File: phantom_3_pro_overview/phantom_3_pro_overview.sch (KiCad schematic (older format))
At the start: 11 parts, among them M1 Brushless_Motor_3phase_seri, M2 Brushless_Motor_3phase_seri, M3 Brushless_Motor_3phase_seri, M4 Brushless_Motor_3phase_seri

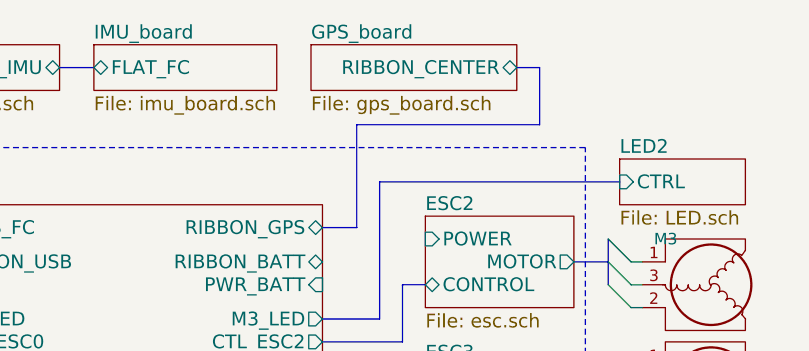
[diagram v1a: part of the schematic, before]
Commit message: Overview: Conceptual schematics of some components.
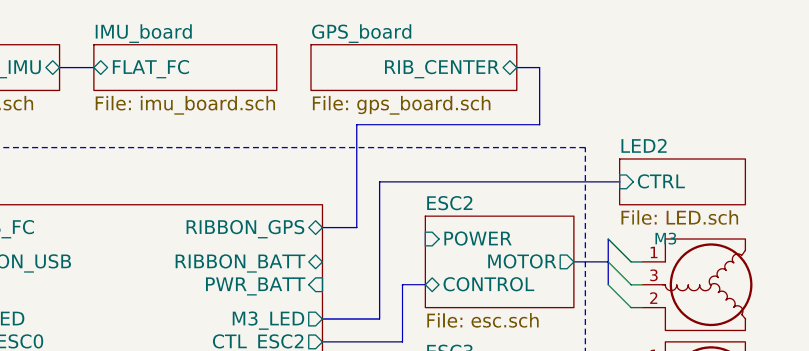
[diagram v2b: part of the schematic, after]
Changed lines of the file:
@@
 LIBS:valves
 LIBS:motors
+LIBS:ic_dil_generic
+LIBS:sensors
+LIBS:u-blox
+LIBS:amplifiers
 LIBS:phantom_3_pro_overview-cache
 EELAYER 25 0
@@
 F0 "GPS_board" 60
 F1 "gps_board.sch" 60
-F2 "RIBBON_CENTER" B R 5000 750 60
+F2 "RIB_CENTER" B R 5000 750 60
 $EndSheet
 $Sheet
@@
 F1 "imu_board.sch" 60
 F2 "FLAT_FC" B L 3150 750 60
-$EndSheet
-$Sheet
-S 1350 1400 650  400
-U 596D582B
-F0 "ESC0" 60
-F1 "esc.sch" 60
-F2 "CONTROL" B R 2000 1700 60
-F3 "POWER" I R 2000 1500 60
-F4 "MOTOR" O L 1350 1600 60
 $EndSheet
 $Sheet
@@
 F3 "FLAT_MOTOR" O L 1700 4600 60
 $EndSheet
+$Sheet
+S 1350 1400 650  400
+U 596D582B
+F0 "ESC0" 60
+F1 "esc.sch" 60
+F2 "CONTROL" B R 2000 1700 60
+F3 "POWER" I R 2000 1500 60
+F4 "MOTOR" O L 1350 1600 60
+$EndSheet
 $EndSCHEMATC

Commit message: Overview: Work on camera and gimbal.
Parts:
- removed M_pitch, M_roll, M_yaw: Motor_Servo, symbol Motor_Servo
- added M_pitch, M_roll, M_yaw: Motor_Servo_3Ph, symbol Motor_Servo_3Ph
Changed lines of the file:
@@
 LIBS:amplifiers
 LIBS:transistors-switches
+LIBS:transistors-power
 LIBS:phantom_3_pro_overview-cache
 EELAYER 25 0
@@
 Entry Bus Bus
 	1400 3000 1500 2900
-$Comp
-L Motor_Servo M_pitch
-U 1 1 5970AE18
-P 1000 5350
-F 0 "M_pitch" H 800 5525 50  0000 L CNN
-F 1 "Motor_Servo" H 800 5190 50  0000 L TNN
-F 2 "" H 1000 5160 50  0001 C CNN
-F 3 "" H 1000 5160 50  0001 C CNN
-	1    1000 5350
-	-1   0    0    1
-$EndComp
 Entry Wire Line
 	1450 5550 1350 5450
@@
 Wire Bus Line
 	1450 5600 1550 5600
-$Comp
-L Motor_Servo M_roll
-U 1 1 5970C2E7
-P 1000 4900
-F 0 "M_roll" H 800 5075 50  0000 L CNN
-F 1 "Motor_Servo" H 800 4740 50  0000 L TNN
-F 2 "" H 1000 4710 50  0001 C CNN
-F 3 "" H 1000 4710 50  0001 C CNN
-	1    1000 4900
-	-1   0    0    1
-$EndComp
 Entry Wire Line
 	1450 5100 1350 5000
@@
 Wire Bus Line
 	1450 5150 1550 5150
-$Comp
-L Motor_Servo M_yaw
-U 1 1 5970C4FE
-P 1000 4350
-F 0 "M_yaw" H 800 4525 50  0000 L CNN
-F 1 "Motor_Servo" H 800 4190 50  0000 L TNN
-F 2 "" H 1000 4160 50  0001 C CNN
-F 3 "" H 1000 4160 50  0001 C CNN
-	1    1000 4350
-	-1   0    0    1
-$EndComp
 Entry Wire Line
 	1450 4550 1350 4450
@@
 Wire Bus Line
 	3300 4450 3150 4450
+$Comp
+L Motor_Servo_3Ph M_yaw
+U 1 1 59719EE0
+P 1000 4350
+F 0 "M_yaw" H 800 4525 50  0000 L CNN
+F 1 "Motor_Servo_3Ph" H 800 4190 50  0000 L TNN
+F 2 "" H 1000 4160 50  0001 C CNN
+F 3 "" H 1000 4160 50  0001 C CNN
+	1    1000 4350
+	-1   0    0    1
+$EndComp
+$Comp
+L Motor_Servo_3Ph M_roll
+U 1 1 5971A5AD
+P 1000 4900
+F 0 "M_roll" H 800 5075 50  0000 L CNN
+F 1 "Motor_Servo_3Ph" H 800 4740 50  0000 L TNN
+F 2 "" H 1000 4710 50  0001 C CNN
+F 3 "" H 1000 4710 50  0001 C CNN
+	1    1000 4900
+	-1   0    0    1
+$EndComp
+$Comp
+L Motor_Servo_3Ph M_pitch
+U 1 1 5971A85D
+P 1000 5350
+F 0 "M_pitch" H 800 5525 50  0000 L CNN
+F 1 "Motor_Servo_3Ph" H 800 5190 50  0000 L TNN
+F 2 "" H 1000 5160 50  0001 C CNN
+F 3 "" H 1000 5160 50  0001 C CNN
+	1    1000 5350
+	-1   0    0    1
+$EndComp
 $EndSCHEMATC

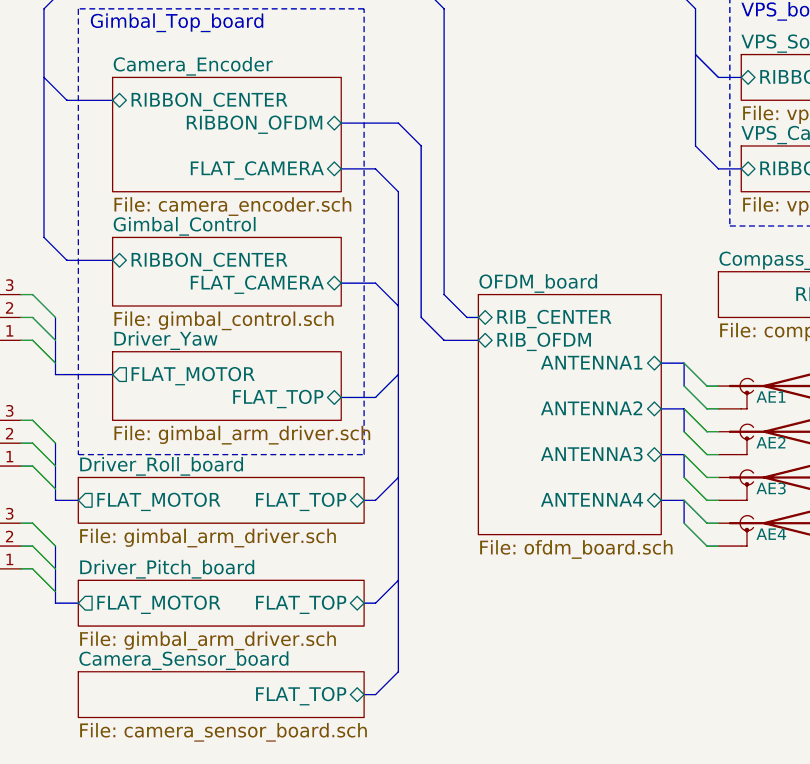
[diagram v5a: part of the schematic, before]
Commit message: Overview: Updated to latest findings.
Added magnetometer to gimbal control, and made some minor fixes.
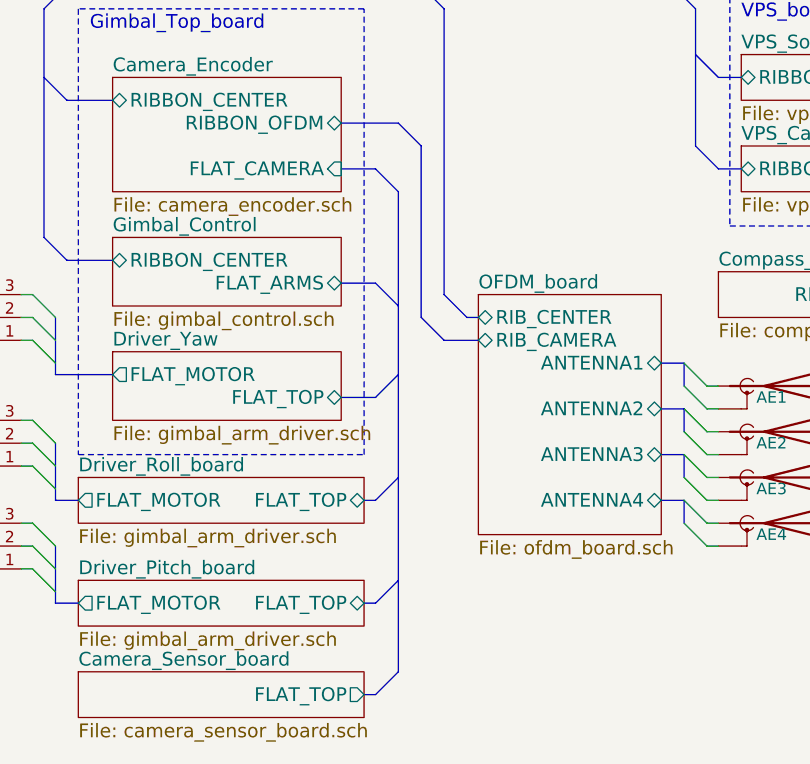
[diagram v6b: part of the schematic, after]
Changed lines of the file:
@@
 F1 "ofdm_board.sch" 60
 F2 "RIB_CENTER" B L 3300 4350 60
-F3 "RIB_OFDM" B L 3300 4450 60
-F4 "ANTENNA1" B R 4100 4550 60
-F5 "ANTENNA2" B R 4100 4750 60
-F6 "ANTENNA3" B R 4100 4950 60
-F7 "ANTENNA4" B R 4100 5150 60
+F3 "ANTENNA1" B R 4100 4550 60
+F4 "ANTENNA2" B R 4100 4750 60
+F5 "ANTENNA3" B R 4100 4950 60
+F6 "ANTENNA4" B R 4100 5150 60
+F7 "RIB_CAMERA" B L 3300 4450 60
 $EndSheet
 $Sheet
@@
 F2 "RIBBON_CENTER" B L 1700 3400 60
 F3 "RIBBON_OFDM" B R 2700 3500 60
-F4 "FLAT_CAMERA" B R 2700 3700 60
+F4 "FLAT_CAMERA" I R 2700 3700 60
 $EndSheet
 $Sheet
@@
 F1 "gimbal_control.sch" 60
 F2 "RIBBON_CENTER" B L 1700 4100 60
-F3 "FLAT_CAMERA" B R 2700 4200 60
+F3 "FLAT_ARMS" B R 2700 4200 60
 $EndSheet
 $Sheet
@@
 F0 "Camera_Sensor_board" 60
 F1 "camera_sensor_board.sch" 60
-F2 "FLAT_TOP" B R 2800 6000 60
+F2 "FLAT_TOP" O R 2800 6000 60
 $EndSheet
 $Comp

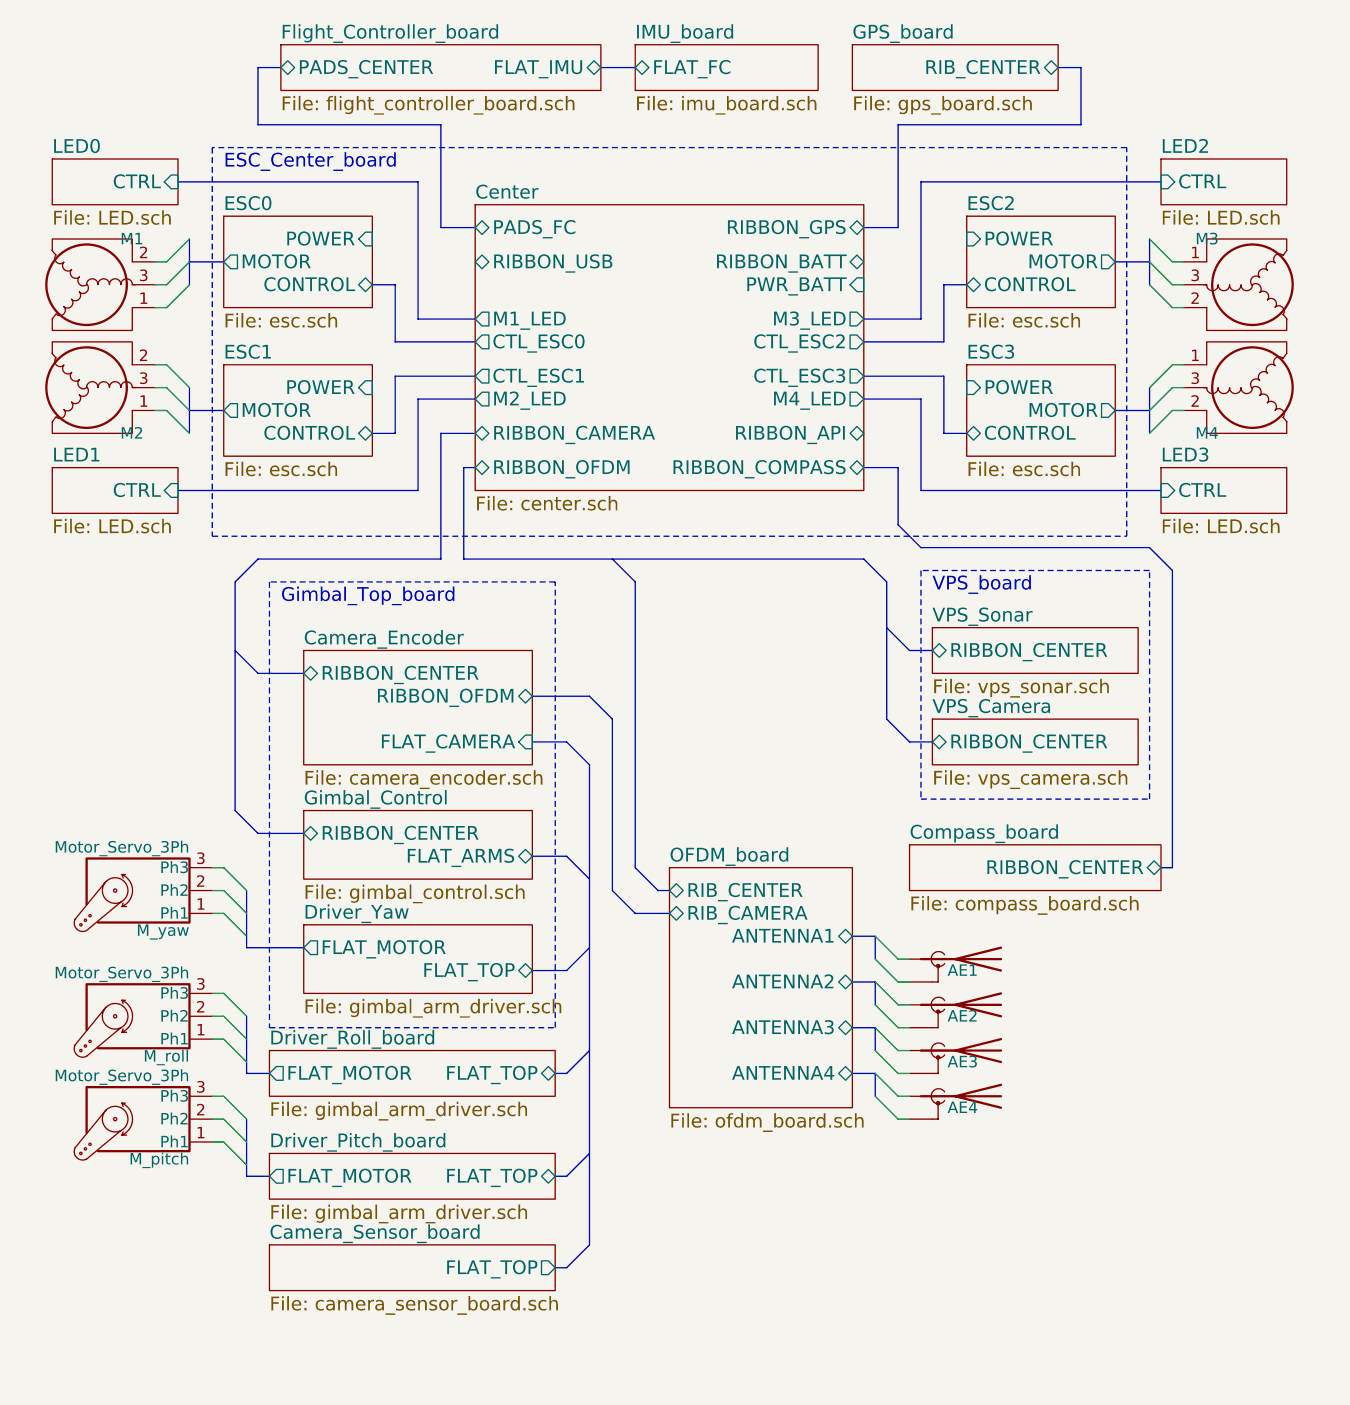
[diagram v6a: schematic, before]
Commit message: Overview: Separated gimbal power circuit.
This is to make sure the connection won't be interpreted as data link.
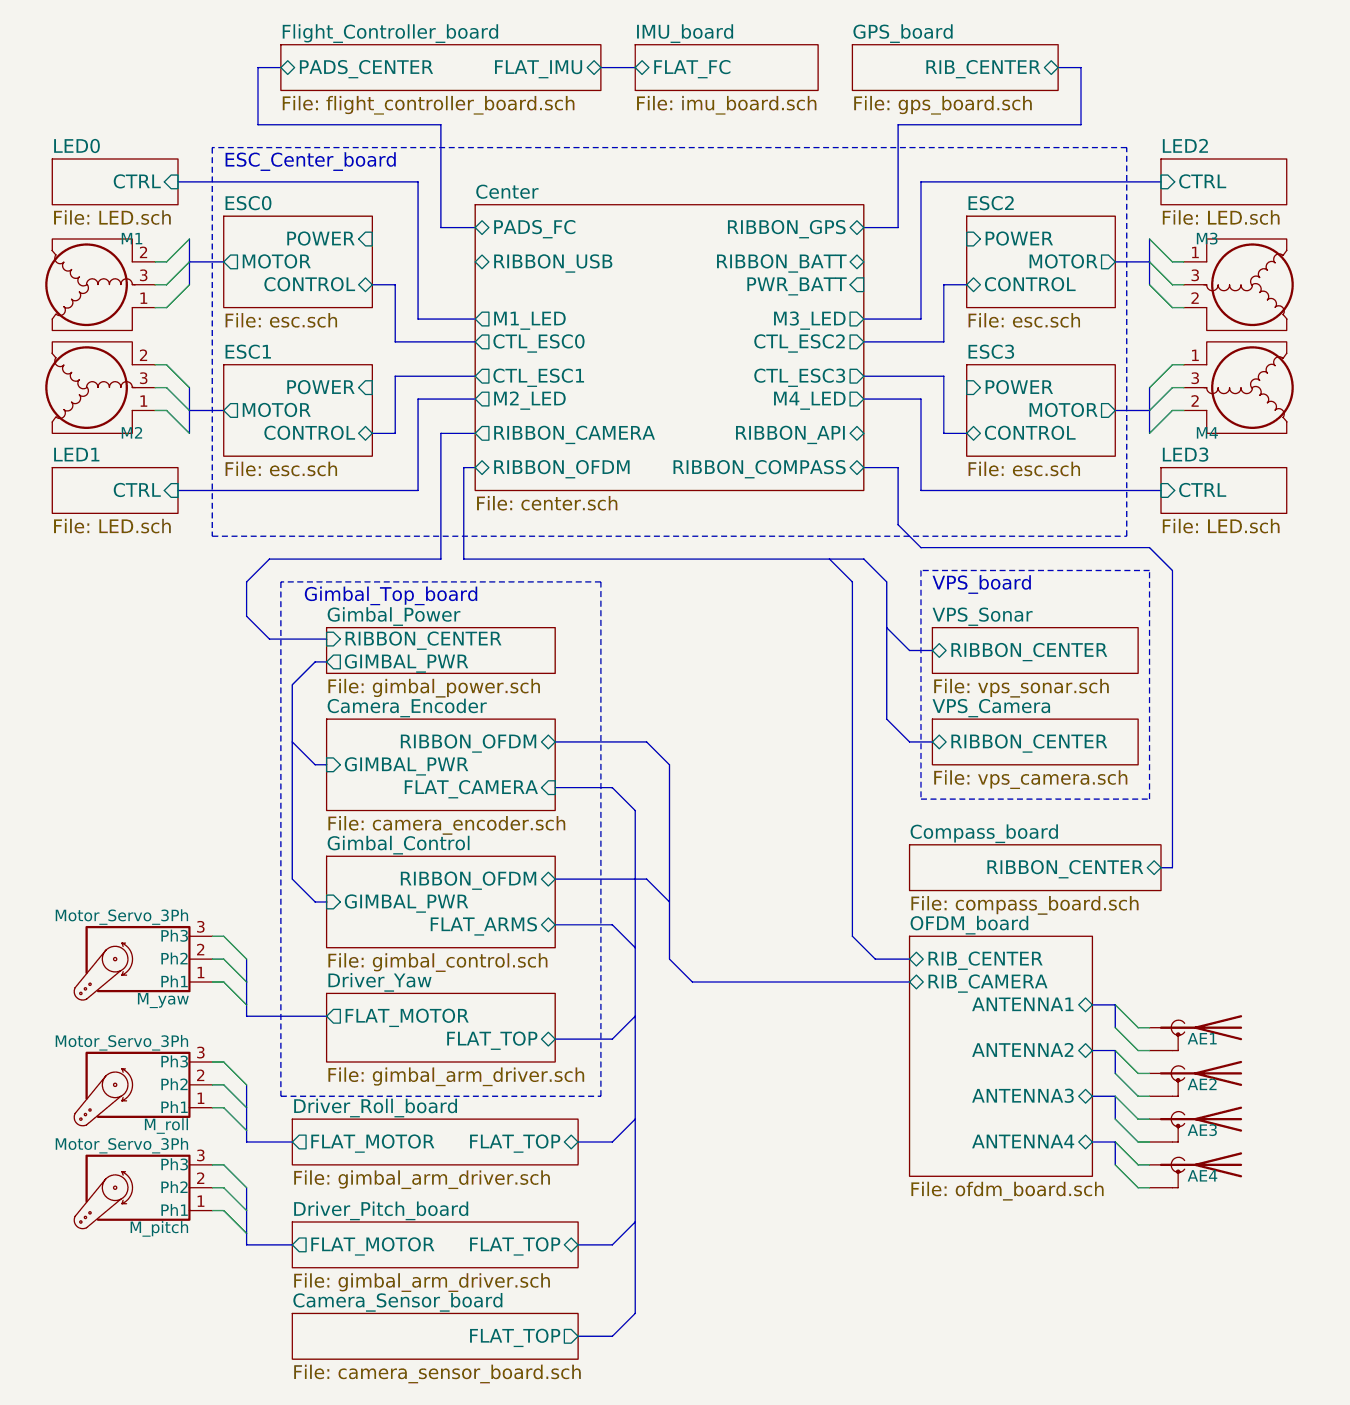
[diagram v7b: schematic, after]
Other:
- moved on the sheet: AE1, AE2, AE3, AE4, M_pitch, M_roll, M_yaw

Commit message: Overview: Upgraded to KiCAD 5.0.1.
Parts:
- AE1, AE2, AE3, AE4: symbol Antenna_Shield -> Device:Antenna_Shield
- M1, M2, M3, M4: symbol Brushless_Motor_3phase_seri -> motors:Brushless_Motor_3phase_seri
- M_pitch, M_roll, M_yaw: symbol Motor_Servo_3Ph -> motors:Motor_Servo_3Ph
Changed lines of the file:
@@
-EESchema Schematic File Version 2
-LIBS:power
-LIBS:device
-LIBS:transistors
-LIBS:conn
-LIBS:linear
-LIBS:regul
-LIBS:74xx
-LIBS:cmos4000
-LIBS:adc-dac
-LIBS:memory
-LIBS:xilinx
-LIBS:microcontrollers
-LIBS:dsp
-LIBS:microchip
-LIBS:analog_switches
-LIBS:motorola
-LIBS:texas
-LIBS:intel
-LIBS:audio
-LIBS:interface
-LIBS:digital-audio
-LIBS:philips
-LIBS:display
-LIBS:cypress
-LIBS:siliconi
-LIBS:opto
-LIBS:atmel
-LIBS:contrib
-LIBS:valves
-LIBS:motors
-LIBS:ic_dil_generic
-LIBS:sensors
-LIBS:u-blox
-LIBS:amplifiers
-LIBS:transistors-switches
-LIBS:transistors-power
-LIBS:sensors-v2
-LIBS:regul-v2
+EESchema Schematic File Version 4
 LIBS:phantom_3_pro_overview-cache
-EELAYER 25 0
+EELAYER 26 0
 EELAYER END
 $Descr User 6614 8268
@@
 $EndSheet
 $Comp
-L Brushless_Motor_3phase_seri M3
+L motors:Brushless_Motor_3phase_seri M3
 U 1 1 596D3599
 P 5850 1700
@@
 $EndComp
 $Comp
-L Brushless_Motor_3phase_seri M4
+L motors:Brushless_Motor_3phase_seri M4
 U 1 1 596D448E
 P 5850 2150
@@
 	5400 2150 5500 2050
 $Comp
-L Brushless_Motor_3phase_seri M2
+L motors:Brushless_Motor_3phase_seri M2
 U 1 1 596DA48B
 P 750 2150
@@
 $EndComp
 $Comp
-L Brushless_Motor_3phase_seri M1
+L motors:Brushless_Motor_3phase_seri M1
 U 1 1 596DA491
 P 750 1700
@@
 	1450 4650 1350 4550
 $Comp
-L Antenna_Shield AE1
+L Device:Antenna_Shield AE1
 U 1 1 597138C4
 P 5600 4950
@@
 	5250 4950 5350 5050
 $Comp
-L Antenna_Shield AE2
+L Device:Antenna_Shield AE2
 U 1 1 5971A63C
 P 5600 5150
@@
 	5250 5150 5350 5250
 $Comp
-L Antenna_Shield AE3
+L Device:Antenna_Shield AE3
 U 1 1 5971A803
 P 5600 5350
@@
 	5250 5350 5350 5450
 $Comp
-L Antenna_Shield AE4
+L Device:Antenna_Shield AE4
 U 1 1 5971A80E
 P 5600 5550
@@
 	4100 4550 4200 4650
 $Comp
-L Motor_Servo_3Ph M_yaw
+L motors:Motor_Servo_3Ph M_yaw
 U 1 1 59719EE0
 P 1000 4650
@@
 $EndComp
 $Comp
-L Motor_Servo_3Ph M_roll
+L motors:Motor_Servo_3Ph M_roll
 U 1 1 5971A5AD
 P 1000 5200
@@
 $EndComp
 $Comp
-L Motor_Servo_3Ph M_pitch
+L motors:Motor_Servo_3Ph M_pitch
 U 1 1 5971A85D
 P 1000 5650
@@
 	4350 3300 4450 3300
 Wire Bus Line
-	4250 3000 4250 3200
-Wire Bus Line
-	4250 3200 4250 3600
-Wire Bus Line
 	2400 2500 2400 2900
 Wire Bus Line
-	2400 2900 4000 2900
-Wire Bus Line
-	4000 2900 4150 2900
-Wire Bus Line
 	1800 4400 1750 4400
 Wire Bus Line
@@
 Wire Bus Line
 	1550 2900 2300 2900
-Wire Bus Line
-	1450 5650 1450 5750
-Wire Bus Line
-	1450 5750 1450 5850
-Wire Bus Line
-	1450 5850 1450 5900
 Wire Wire Line
 	1350 5750 1300 5750
@@
 Wire Bus Line
 	1450 5900 1650 5900
-Wire Bus Line
-	1450 5200 1450 5300
-Wire Bus Line
-	1450 5300 1450 5400
-Wire Bus Line
-	1450 5400 1450 5450
 Wire Wire Line
 	1350 5300 1300 5300
@@
 Wire Bus Line
 	1450 5450 1650 5450
-Wire Bus Line
-	1450 4650 1450 4750
-Wire Bus Line
-	1450 4750 1450 4850
-Wire Bus Line
-	1450 4850 1450 4900
 Wire Wire Line
 	1350 4750 1300 4750
@@
 	2800 3900 3050 3900
 Wire Bus Line
-	3150 4000 3150 4600
-Wire Bus Line
-	3150 4600 3150 4900
-Wire Bus Line
-	3150 4900 3150 5350
-Wire Bus Line
-	3150 5350 3150 5800
-Wire Bus Line
-	3150 5800 3150 6200
-Wire Bus Line
-	3300 3800 3300 4400
-Wire Bus Line
-	3300 4400 3300 4650
-Wire Bus Line
 	4350 4650 4200 4650
 Wire Bus Line
@@
 	1800 3350 1750 3350
 Wire Bus Line
-	1650 3450 1650 3700
-Wire Bus Line
-	1650 3700 1650 4300
-Wire Bus Line
 	1800 3800 1750 3800
 Wire Bus Line
@@
 Wire Bus Line
 	3200 4300 2800 4300
+Wire Bus Line
+	4250 3000 4250 3600
+Wire Bus Line
+	2400 2900 4150 2900
+Wire Bus Line
+	3300 3800 3300 4650
+Wire Bus Line
+	1650 3450 1650 4300
+Wire Bus Line
+	1450 5650 1450 5900
+Wire Bus Line
+	1450 5200 1450 5450
+Wire Bus Line
+	1450 4650 1450 4900
+Wire Bus Line
+	3150 4000 3150 6200
 $EndSCHEMATC
